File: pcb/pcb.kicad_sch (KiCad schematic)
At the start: 53 parts, among them J1 OLED, SW1 Rotary_Encoder_Switch, U1 Elite-C

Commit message: Added initial modified files.
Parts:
- removed D1, D10, D11, D12, D13, D14, D15, D16, D2, D3, D4, D5, D6, D7, D8, D9: BAV70, Keebio-Parts:SOT-23_Handsoldering, symbol Diode:BAV70
- removed MX00, MX10, MX11, MX12, MX13, MX20, MX21, MX22, MX23, MX30, MX31, MX32, MX33, MX40, MX41, MX42, MX43, MX50, MX51, MX52, MX53, MX60, MX61, MX62, MX63, MX71, MX72: MX-NoLED, MX_Only:MXOnly-1U-Hotswap, symbol MX_Alps_Hybrid:MX-NoLED
- removed MX01: MX-NoLED, MX_Only:MXOnly-1.5U-Hotswap, symbol MX_Alps_Hybrid:MX-NoLED
- removed MX02: MX-NoLED, MX_Only:MXOnly-1.75U-Hotswap, symbol MX_Alps_Hybrid:MX-NoLED
- removed MX03: MX-NoLED, MX_Only:MXOnly-2.25U-Hotswap, symbol MX_Alps_Hybrid:MX-NoLED
- added D? (x33): D_Small, symbol Device:D_Small
- added MX? (x33): MX-NoLED, symbol MX_Alps_Hybrid:MX-NoLED
- added SW?: Rotary_Encoder_Switch, Rotary_Encoder:RotaryEncoder_Alps_EC11E-Switch_Vertical_H20mm, symbol Device:Rotary_Encoder_Switch
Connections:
- net ENA: no longer U1.8 (5/PC6)
- net ENB: no longer U1.9 (6/PD7)
- net GND: now also SW?.C
- net SCL: no longer U1.6 (3/PD0)
- net SDA: no longer U1.5 (2/PD1)
- net Col0: no longer names the net of U1.1 (TX0/PD3)
- net Col1: no longer names the net of U1.2 (RX1/PD2)
- net Col2: no longer names the net of U1.20 (A3/PF4)
- net Col3: no longer names the net of U1.19 (A2/PF5)
- net Col4: no longer names the net of U1.18 (A1/PF6)
- net Col5: no longer names the net of U1.17 (A0/PF7)
- net Col6: no longer names the net of U1.16 (15/PB1)
- net Col7: no longer names the net of U1.10 (7/PE6)
- net Col7: no longer SW1.S1
- net Row0: no longer names the net of U1.7 (4/PD4)
- net Row1: no longer names the net of U1.12 (9/PB5)
- net Row2: no longer names the net of U1.11 (8/PB4)
- net Row3: no longer names the net of U1.13 (10/PB6)
- new net: D?.2 (A), MX?.2 (ROW) (x33)
- new net COL0: MX?.1 (COL), MX?.1 (COL), MX?.1 (COL), MX?.1 (COL), MX?.1 (COL), MX?.1 (COL)
- new net COL1: MX?.1 (COL), MX?.1 (COL), MX?.1 (COL), MX?.1 (COL), MX?.1 (COL), MX?.1 (COL)
- new net COL2: MX?.1 (COL), MX?.1 (COL), MX?.1 (COL), MX?.1 (COL), MX?.1 (COL), MX?.1 (COL)
- new net COL3: MX?.1 (COL), MX?.1 (COL), MX?.1 (COL), MX?.1 (COL), MX?.1 (COL)
- new net COL4: MX?.1 (COL), MX?.1 (COL), MX?.1 (COL), MX?.1 (COL), MX?.1 (COL)
- new net COL5: MX?.1 (COL), MX?.1 (COL), MX?.1 (COL), MX?.1 (COL), MX?.1 (COL)
- new net ENC: SW?.B
- new net END: SW?.A
- new net ROW0: D?.1 (K), D?.1 (K), D?.1 (K), D?.1 (K), D?.1 (K), D?.1 (K)
- new net ROW1: D?.1 (K), D?.1 (K), D?.1 (K), D?.1 (K), D?.1 (K), D?.1 (K)
- new net ROW2: D?.1 (K), D?.1 (K), D?.1 (K), D?.1 (K), D?.1 (K), D?.1 (K)
- new net ROW3: D?.1 (K), D?.1 (K), D?.1 (K), D?.1 (K), D?.1 (K), D?.1 (K)
- new net ROW4: D?.1 (K), D?.1 (K), D?.1 (K), D?.1 (K), D?.1 (K), D?.1 (K)
- new net ROW5: D?.1 (K), D?.1 (K), D?.1 (K)
- no-connect marks 10 -> 9
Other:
- note added: "ENCODERS"
- note added: "MATRIX"
- note added: "MCU"
- note added: "MOUNTING HOLES"
- note added: "OLED"
- note added: "UNDERGLOW"
- moved on the sheet: H1, H2, H3, H4, J1, SW1, U1

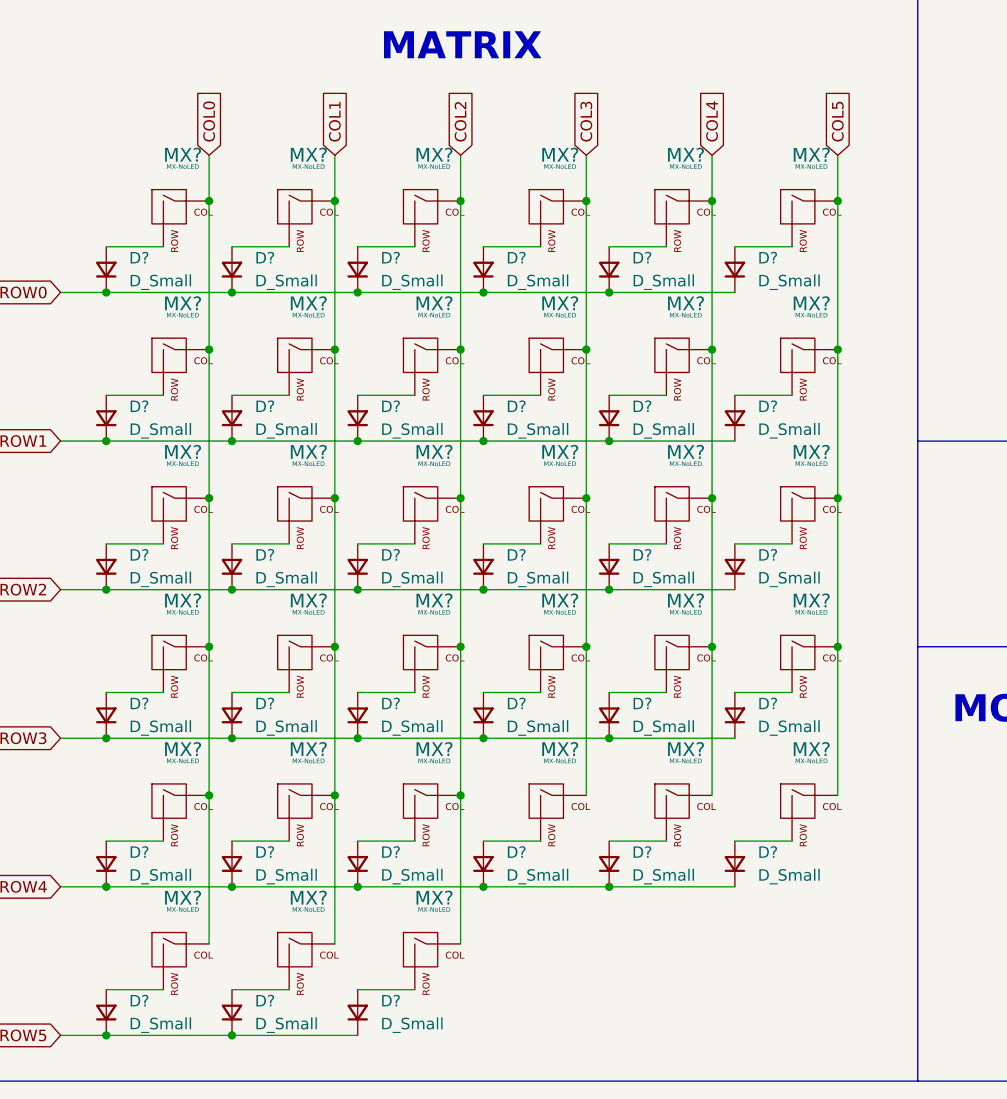
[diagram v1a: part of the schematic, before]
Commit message: Added keyboard matrix references.
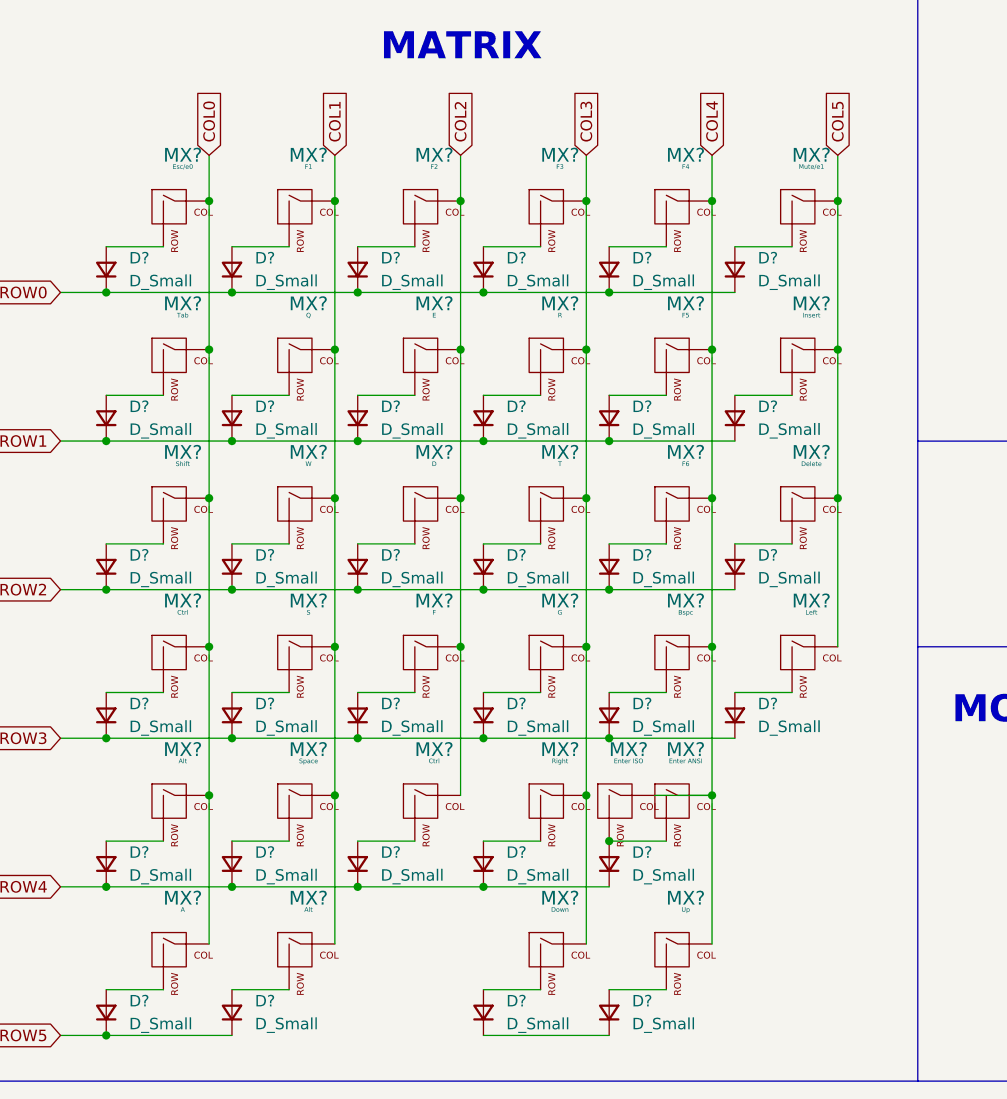
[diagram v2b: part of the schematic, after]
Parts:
- removed D? (x3): D_Small, symbol Device:D_Small
- removed MX? (x3): MX-NoLED, symbol MX_Alps_Hybrid:MX-NoLED
- added D? (x3): D_Small, symbol Device:D_Small
- added MX?: Up, symbol MX_Alps_Hybrid:MX-NoLED
- added MX?: Down, symbol MX_Alps_Hybrid:MX-NoLED
- added MX?: Left, symbol MX_Alps_Hybrid:MX-NoLED
- added MX?: Enter ISO, symbol MX_Alps_Hybrid:MX-NoLED
- MX?: value MX-NoLED -> A
- MX?: value MX-NoLED -> R
- MX?: value MX-NoLED -> Enter ANSI
- MX?: value MX-NoLED -> F6
- MX?: value MX-NoLED -> Esc/e0
- MX?: value MX-NoLED -> Space
- MX?: value MX-NoLED -> G
- MX?: value MX-NoLED -> F5
- MX?: value MX-NoLED -> Shift
- MX?: value MX-NoLED -> F
- MX?: value MX-NoLED -> W
- MX?: value MX-NoLED -> F4
- MX?: value MX-NoLED -> F3
- MX?: value MX-NoLED -> Delete
- MX? (x2): value MX-NoLED -> Alt
- MX?: value MX-NoLED -> F1
- MX?: value MX-NoLED -> Mute/e1
- MX? (x2): value MX-NoLED -> Ctrl
- MX?: value MX-NoLED -> D
- MX?: value MX-NoLED -> E
- MX?: value MX-NoLED -> Right
- MX?: value MX-NoLED -> Tab
- MX?: value MX-NoLED -> Bspc
- MX?: value MX-NoLED -> T
- MX?: value MX-NoLED -> Q
- MX?: value MX-NoLED -> F2
- MX?: value MX-NoLED -> S
- MX?: value MX-NoLED -> Insert
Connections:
- net COL3: now also MX?.1 (COL)
- net COL4: now also MX?.1 (COL), MX?.1 (COL)
- net COL5: now also MX?.1 (COL)
- net ROW3: now also D?.1 (K)
- net at D?.2 (A), MX?.2 (ROW): now also MX?.2 (ROW)
- new net: D?.2 (A), MX?.2 (ROW) (x3)
- new net: D?.1 (K), D?.1 (K)

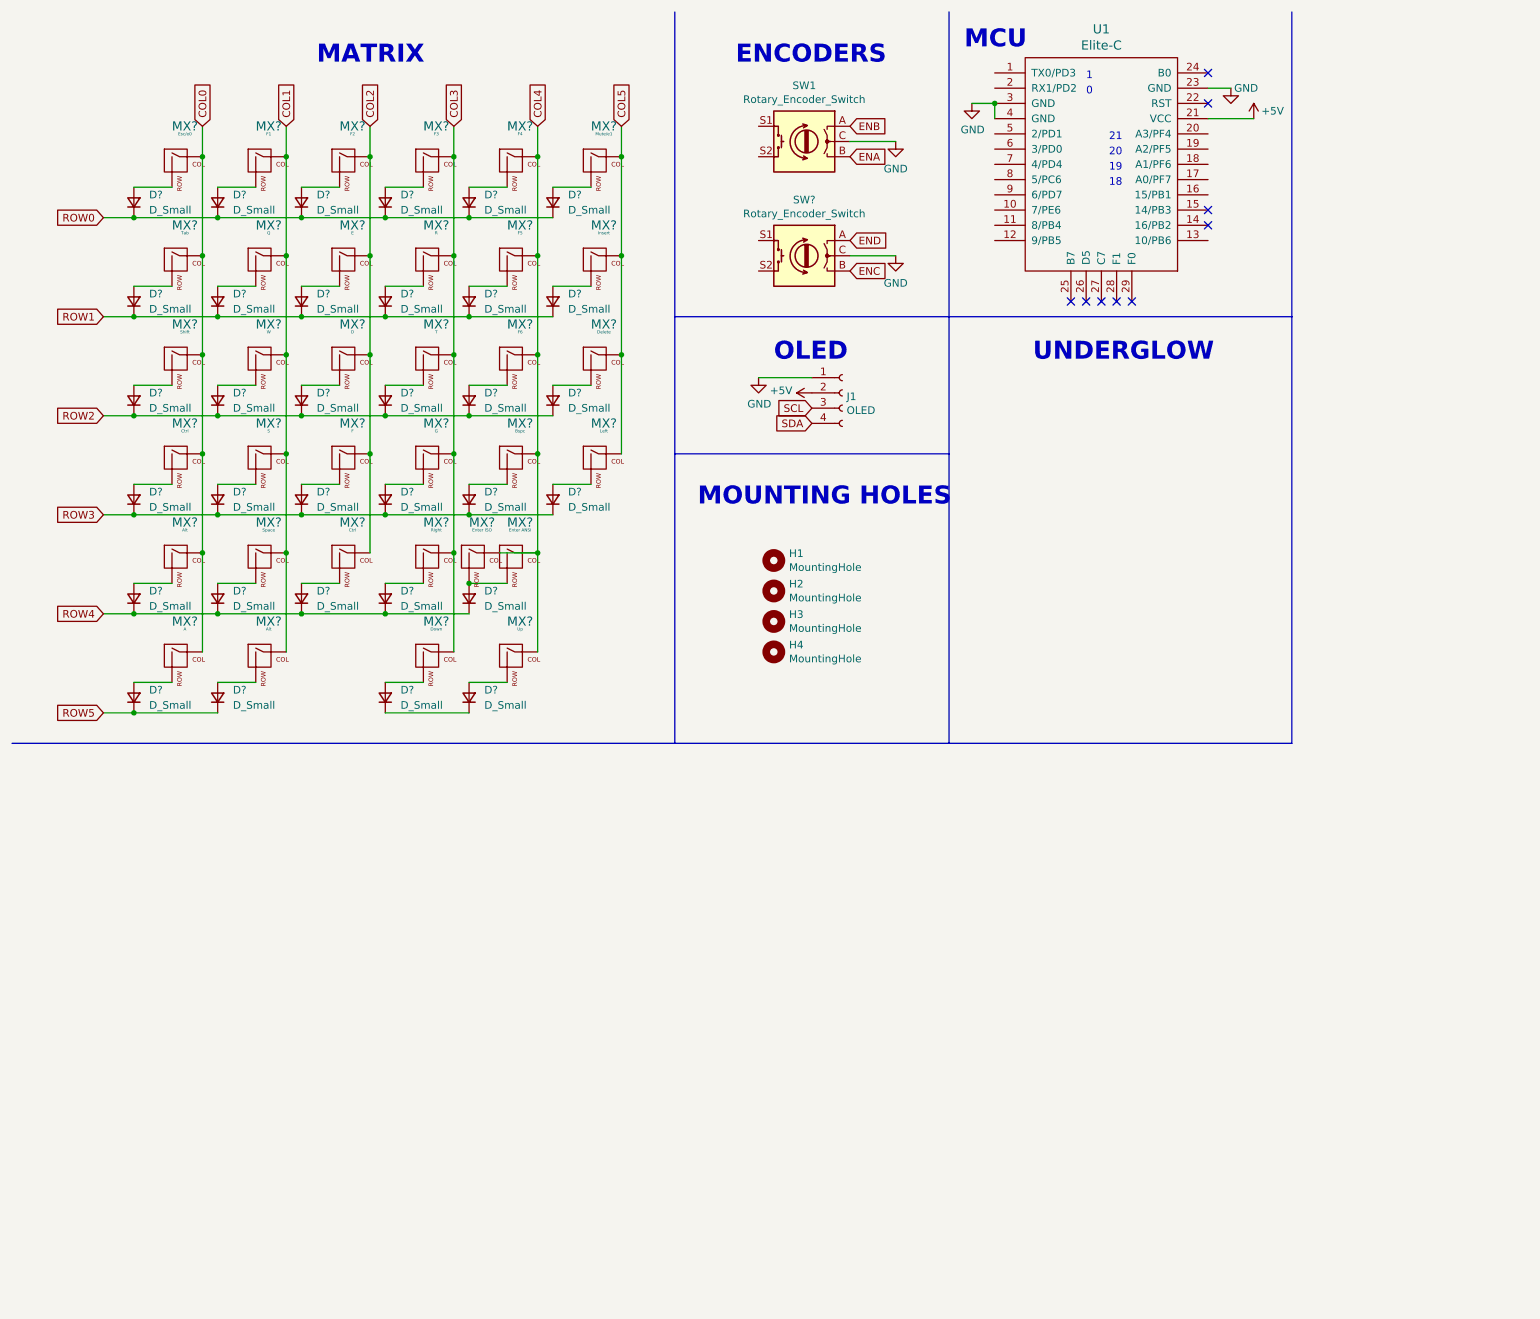
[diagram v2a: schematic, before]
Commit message: Finished tentative schematic and imported footprints into the PCB file.
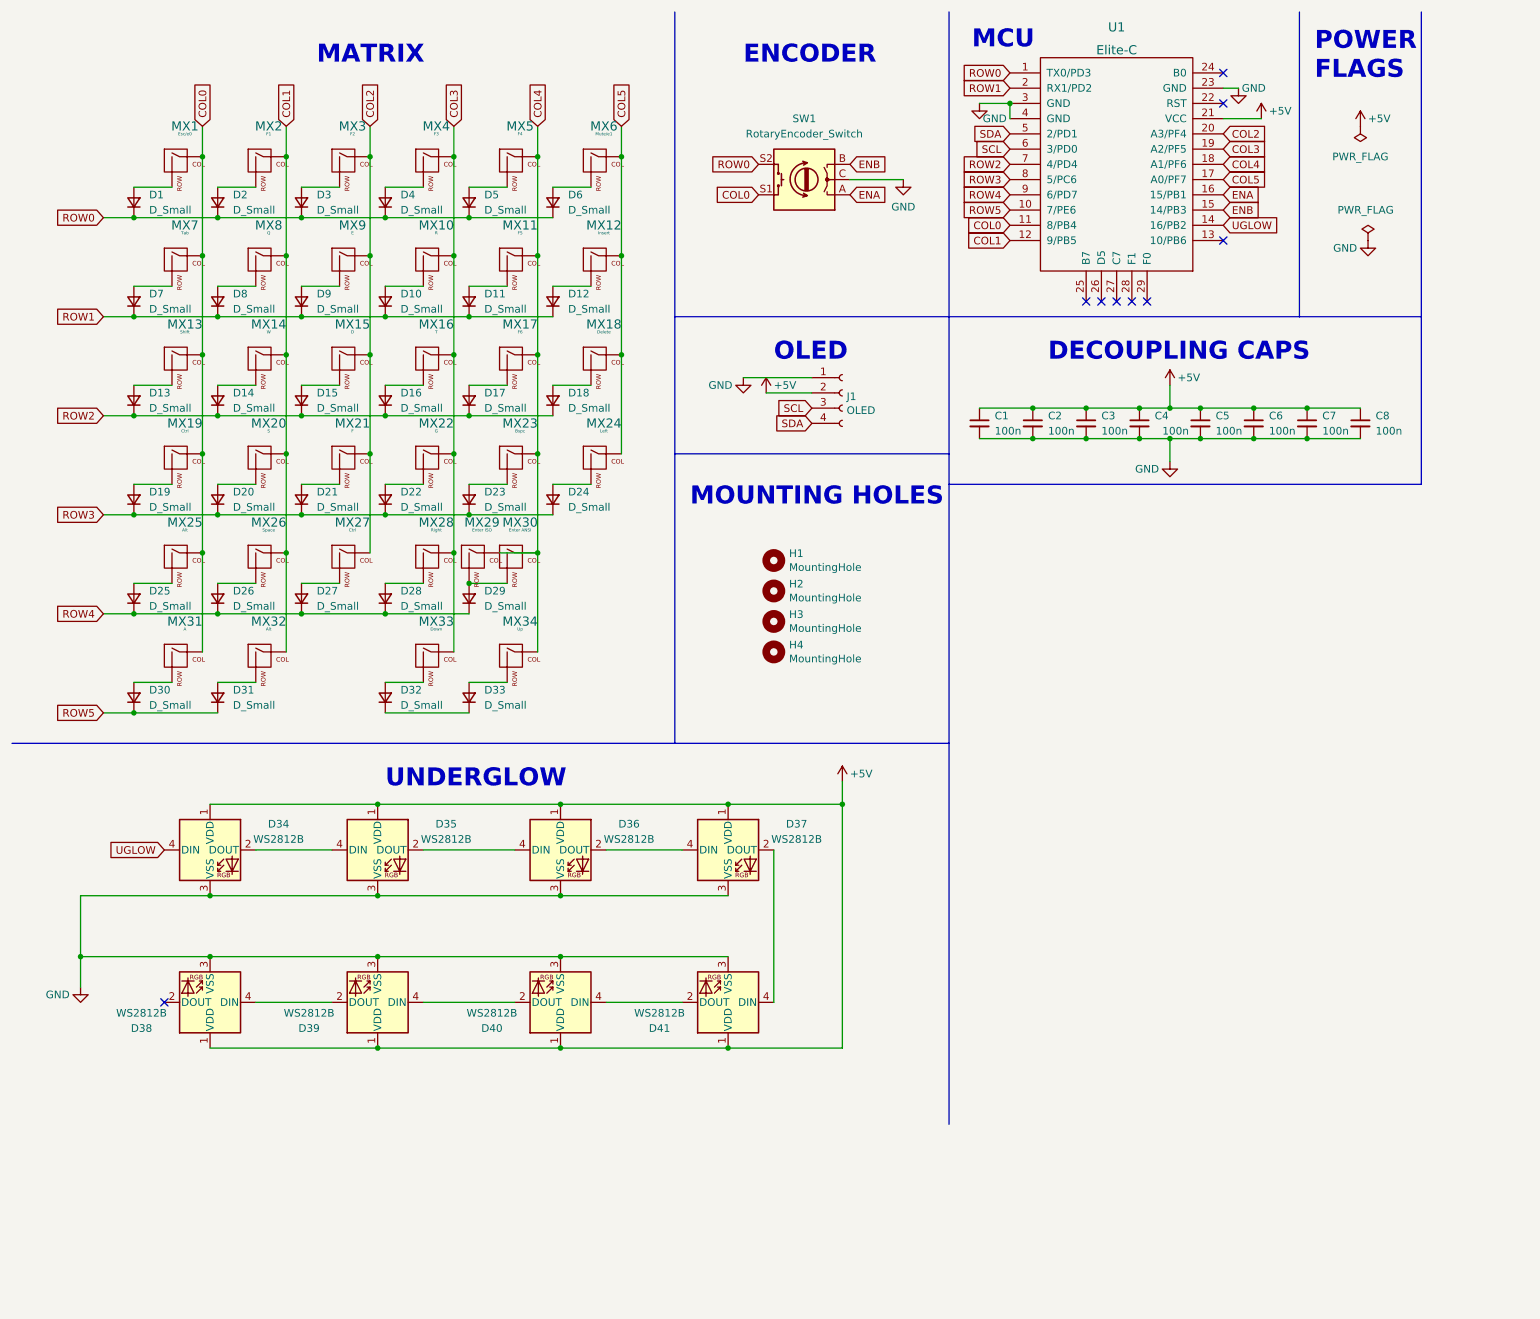
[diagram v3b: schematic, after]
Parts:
- removed SW1, SW?: Rotary_Encoder_Switch, Rotary_Encoder:RotaryEncoder_Alps_EC11E-Switch_Vertical_H20mm, symbol Device:Rotary_Encoder_Switch
- removed U1: Elite-C, Keebio-Parts:Elite-C, symbol sketchy-rescue:Elite-C-keebio-sketchy-rescue
- added C1, C2, C3, C4, C5, C6, C7, C8: 100n, Capacitor_SMD:C_0805_2012Metric_Pad1.18x1.45mm_HandSolder, symbol Device:C_Small
- added D34, D35, D36, D37, D38, D39, D40, D41: WS2812B, LED_SMD:LED_WS2812B_PLCC4_5.0x5.0mm_P3.2mm, symbol LED:WS2812B
- added SW1: RotaryEncoder_Switch, Rotary_Encoder:RotaryEncoder_Alps_EC11E-Switch_Vertical_H20mm, symbol Device:RotaryEncoder_Switch
- added U1: Elite-C, Keebio-Parts:Elite-C, symbol keebio:Elite-C
- D1, D10, D11, D12, D13, D14, D15, D16, D17, D18, D19, D2, D20, D21, D22, D23, D24, D25, D26, D27, D28, D29, D3, D30, D31, D32, D33, D4, D5, D6, D7, D8, D9: renamed from D?; footprint (none) -> custom_parts:Diode-dual-onesided
- MX1, MX10, MX11, MX12, MX13, MX14, MX15, MX16, MX17, MX18, MX19, MX2, MX20, MX21, MX22, MX23, MX24, MX25, MX26, MX27, MX28, MX29, MX3, MX30, MX31, MX32, MX33, MX34, MX4, MX5, MX6, MX7, MX8, MX9: renamed from MX?; footprint (none) -> acheron_MXH_metalrings:MX100H
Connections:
- net +5V: now also C1.1, C2.1, C3.1, C4.1, C5.1, C6.1, C7.1, C8.1, D34.1 (VDD), D35.1 (VDD), D36.1 (VDD), D37.1 (VDD), D38.1 (VDD), D39.1 (VDD), D40.1 (VDD), D41.1 (VDD), U1.21 (VCC)
- net COL0: now also SW1.S1, U1.11 (8/PB4)
- net COL1: now also U1.12 (9/PB5)
- net COL2: now also U1.20 (A3/PF4)
- net COL3: now also U1.19 (A2/PF5)
- net COL4: now also U1.18 (A1/PF6)
- net COL5: now also U1.17 (A0/PF7)
- net ENA: now also SW1.A, U1.16 (15/PB1)
- net ENB: now also SW1.B, U1.15 (14/PB3)
- net GND: now also C1.2, C2.2, C3.2, C4.2, C5.2, C6.2, C7.2, C8.2, D34.3 (VSS), D35.3 (VSS), D36.3 (VSS), D37.3 (VSS), D38.3 (VSS), D39.3 (VSS), D40.3 (VSS), D41.3 (VSS), SW1.C, U1.23 (GND), U1.3 (GND), U1.4 (GND)
- net ROW0: now also SW1.S2, U1.1 (TX0/PD3)
- net ROW1: now also U1.2 (RX1/PD2)
- net ROW2: now also U1.7 (4/PD4)
- net ROW3: now also U1.8 (5/PC6)
- net ROW4: now also U1.9 (6/PD7)
- net ROW5: now also U1.10 (7/PE6)
- net SCL: now also U1.6 (3/PD0)
- net SDA: now also U1.5 (2/PD1)
- new net: D37.2 (DOUT), D41.4 (DIN)
- new net: D36.2 (DOUT), D37.4 (DIN)
- new net: D39.4 (DIN), D40.2 (DOUT)
- new net: D40.4 (DIN), D41.2 (DOUT)
- new net: D38.4 (DIN), D39.2 (DOUT)
- new net: D35.2 (DOUT), D36.4 (DIN)
- new net: D34.2 (DOUT), D35.4 (DIN)
- new net UGLOW: D34.4 (DIN), U1.14 (16/PB2)
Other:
- note added: "DECOUPLING CAPS"
- note added: "ENCODER"
- note added: "POWER FLAGS"
- note removed: "0"
- note removed: "1"
- note removed: "18"
- note removed: "19"
- note removed: "20"
- note removed: "21"
- note removed: "ENCODERS"

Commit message: Modified Elite-C footprint.
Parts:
- U1: footprint Keebio-Parts:Elite-C -> Keebio-Parts:Elite-C-castellated-29pin-holes
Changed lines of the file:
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@@
       (effects (font (size 1.524 1.524)))
     )
-    (property "Footprint" "Keebio-Parts:Elite-C" (id 2) (at 223.52 100.33 90)
+    (property "Footprint" "Keebio-Parts:Elite-C-castellated-29pin-holes" (id 2) (at 223.52 100.33 90)
       (effects (font (size 1.524 1.524)) hide)
     )
@@
     )
     (path "/45e43045-7dd0-4e88-82a6-613fa4322bc2"
-      (reference "U1") (unit 1) (value "Elite-C") (footprint "Keebio-Parts:Elite-C")
-    )
-  )
+      (reference "U1") (unit 1) (value "Elite-C") (footprint "Keebio-Parts:Elite-C-castellated-29pin-holes")
+    )
+  )
